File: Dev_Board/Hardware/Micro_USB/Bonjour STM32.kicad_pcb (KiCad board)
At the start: 2 copper layers, 50 x 70 mm, 68 parts, among them J11 IPS_SWITCH, Q1 S8050, Q2 S8050, Q3 S8050, SW1 SW_Push, SW2 SW_Push, SW3 SW_Push, U3 STM32F401RCTx

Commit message: Update PCB design
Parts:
- added G***: LOGO, Logo:emoe, B.Cu at (185.2, 104.5)
- added G***: LOGO, Logo:单片姬, F.Cu at (185.3, 83.0)
- added REF**: OSHW-Logo2_9.8x8mm_SilkScreen, Symbol:OSHW-Logo2_9.8x8mm_SilkScreen, B.Cu at (172.8, 63.5)
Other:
- board text added: "EEPROM"
- board text added: "Encoder"
- board text added: "FLASH"
- board text added: "I2C1"
- board text added: "I2C_2"
- board text added: "RX"
- board text added: "SPI1"
- board text added: "SPI_2"
- board text added: "TIM1_CH1/2"
- board text added: "TX"

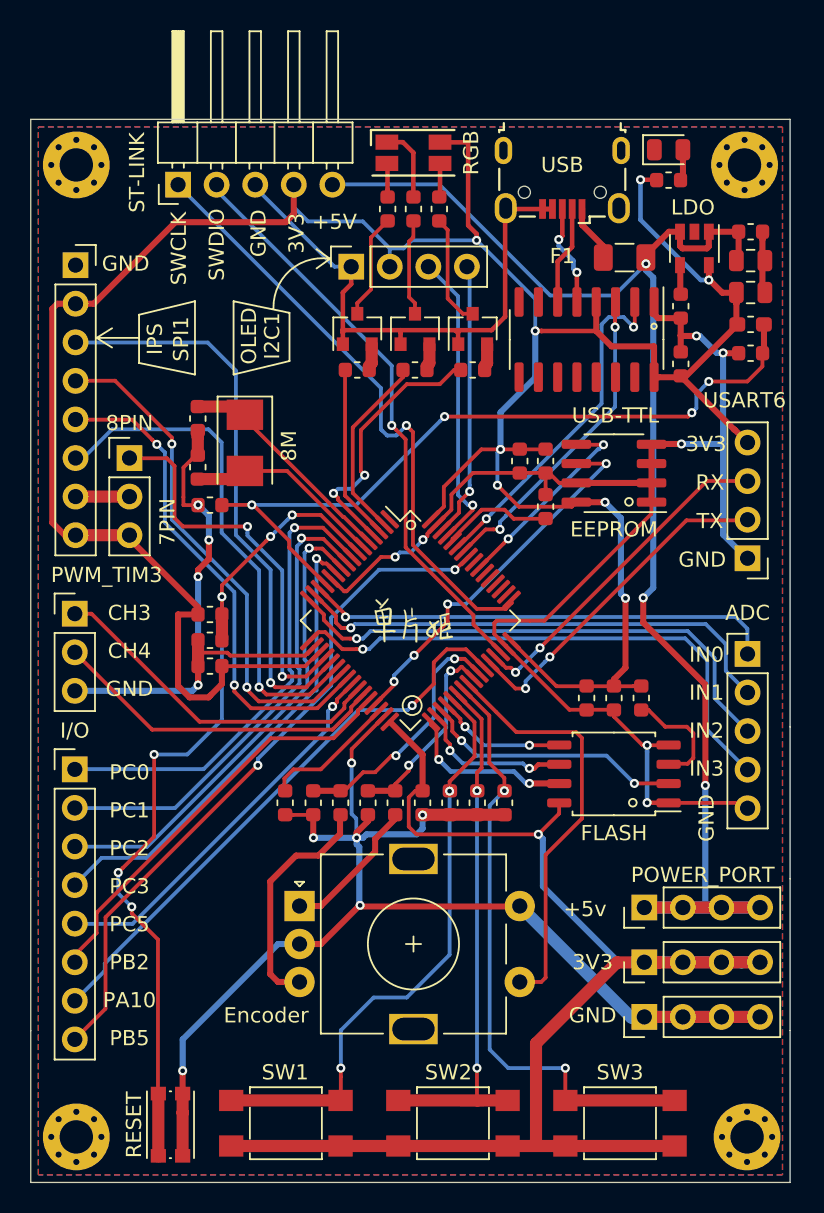
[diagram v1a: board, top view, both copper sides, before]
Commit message: fix footprint bug & add QR Code
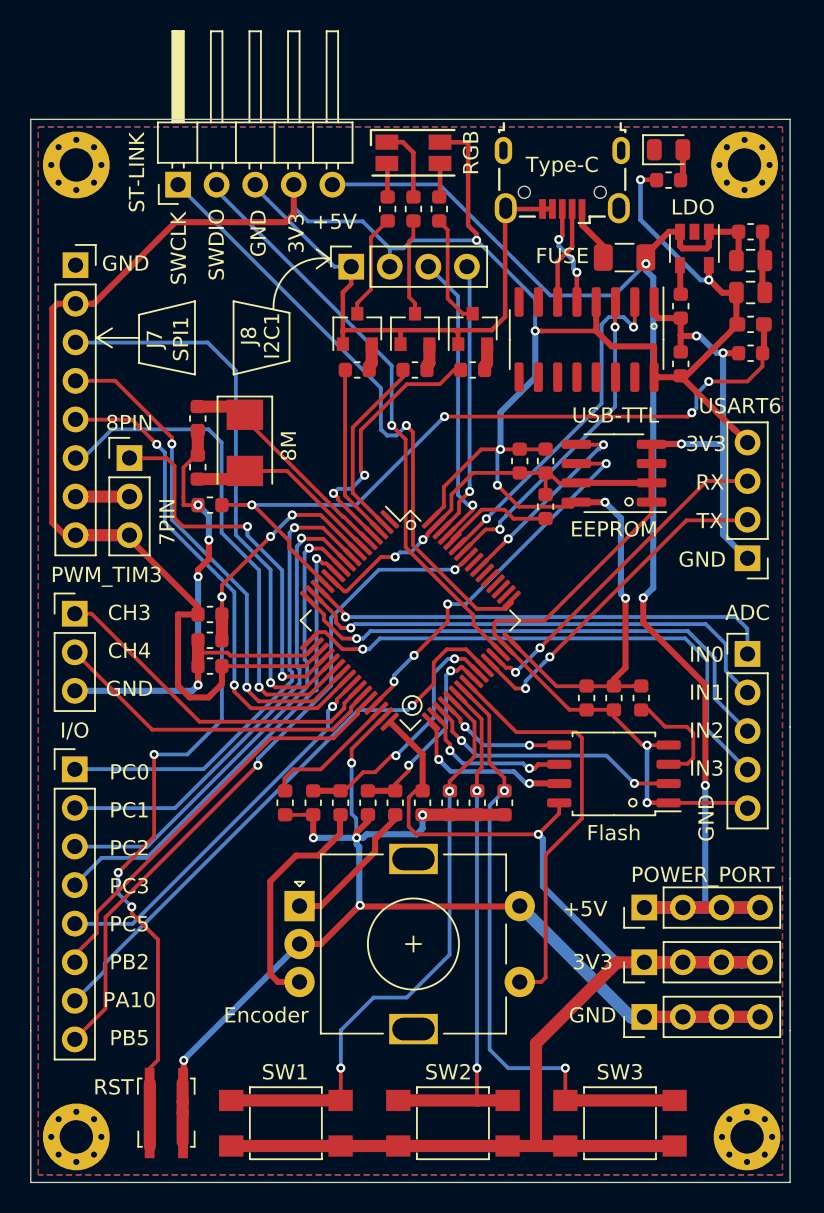
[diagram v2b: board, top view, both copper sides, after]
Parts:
- removed G***: LOGO, Logo:emoe
- removed G***: LOGO, Logo:单片姬
- removed REF**: OSHW-Logo2_9.8x8mm_SilkScreen, Symbol:OSHW-Logo2_9.8x8mm_SilkScreen
- RST: renamed from RESET; footprint Button_Switch_SMD:SW_Push_1P1T_NO_CK_KMR2 -> Button_Switch_SMD:Button_SMD_3mmx4mmx2.5mm
- moved RST 0.80 mm to (169.0, 115.4)
- renumbered +5v to +5V, F1 to FUSE, FLASH to Flash, IPS to J7, OLED to J8, USB to Type-C
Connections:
- Encoder pad MP: GND -> (no net)
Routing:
- net GND: track 270.7 -> 269.9 mm
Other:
- board text added: "TIM1_CH1&2"
- board text removed: "TIM1_CH1/2"

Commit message: Fix Fatal Error on PCB Design
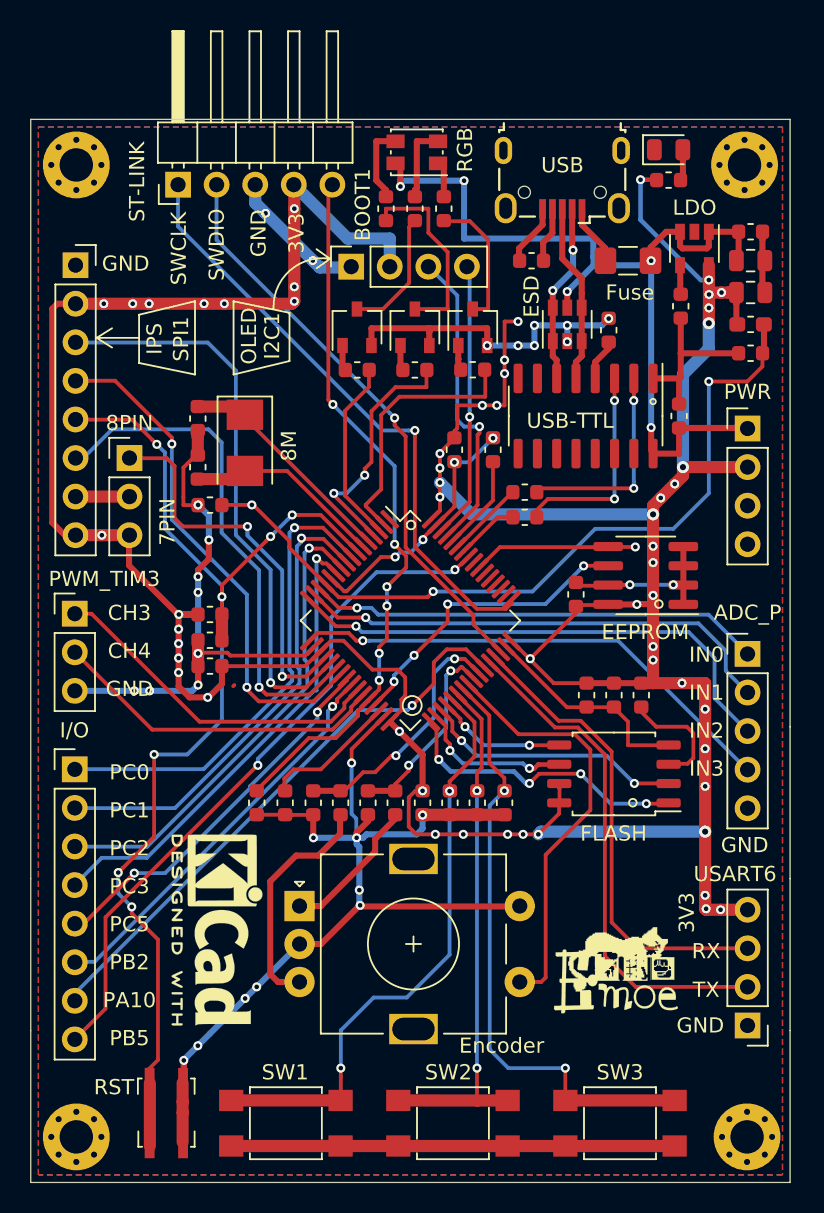
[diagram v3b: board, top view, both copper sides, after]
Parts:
- removed 3V3: 3V3, Connector_PinHeader_2.54mm:PinHeader_1x04_P2.54mm_Vertical
- removed GND: GND, Connector_PinHeader_2.54mm:PinHeader_1x04_P2.54mm_Vertical
- removed RGB: LED_RGBA, LED_SMD:LED_RGB_1210
- added C22: 104, Capacitor_SMD:C_0603_1608Metric, F.Cu at (202.7, 69.5)
- added D2: LED_RABG, LED_SMD:LED_Kingbright_AAA3528ESGCT, F.Cu at (185.4, 52.2)
- added G***: LOGO, Logo:emoe, F.Cu at (198.6, 106.3)
- added R12: 4.7k, Resistor_SMD:R_0603_1608Metric, F.Cu at (192.5, 76.2)
- added R13: 4.7k, Resistor_SMD:R_0603_1608Metric, F.Cu at (192.5, 74.5)
- added R14: 10k, Resistor_SMD:R_0603_1608Metric, F.Cu at (193.0, 59.3)
- added R15: 10k, Resistor_SMD:R_0603_1608Metric, F.Cu at (174.9, 95.0)
- added REF**: Symbol_GNU-Logo_SilkscreenTop, Symbol:Symbol_GNU-Logo_SilkscreenTop, B.Cu at (198.7, 103.8)
- added REF**: OSHW-Logo2_9.8x8mm_SilkScreen, Symbol:OSHW-Logo2_9.8x8mm_SilkScreen, B.Cu at (172.0, 106.6)
- added REF**: KiCad-Logo2_5mm_SilkScreen, Symbol:KiCad-Logo2_5mm_SilkScreen, F.Cu at (172.3, 103.4)
- added U6: USBLC6-2SC6, Package_TO_SOT_SMD:SOT-23-6, F.Cu at (195.3, 63.5)
- F1: renamed from FUSE; footprint Fuse:Fuse_1206_3216Metric -> Fuse:Fuse_1206_3216Metric_Pad1.42x1.75mm_HandSolder
- Q1, Q2, Q3: value S8050 -> S8050-SOT23; footprint Package_TO_SOT_SMD:SOT-23 -> Package_TO_SOT_SMD:SOT-23W
- moved J12 32.3 mm to (207.2, 70.4), turned to 0 degrees
- moved J6 30.8 mm to (207.2, 109.7)
- moved C20 9.00 mm to (195.9, 81.3), turned to 90 degrees
- moved U5 7.05 mm to (200.5, 80.0)
- moved C1 5.24 mm to (198.1, 63.9)
- moved R0 5.10 mm to (190.4, 71.8)
- moved U1 5.03 mm to (196.5, 69.5)
- moved C15 4.37 mm to (187.9, 71.8)
- moved Q3 3.81 mm to (185.3, 63.7)
- moved R10 3.81 mm to (185.3, 66.5), turned to 0 degrees
- moved Q1 3.80 mm to (189.1, 63.7)
- moved R5 3.80 mm to (189.1, 66.5), turned to 0 degrees
- moved R9 3.51 mm to (183.4, 55.9)
- moved R7 2.00 mm to (187.2, 55.9)
- moved R8 1.79 mm to (185.3, 55.9)
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- renumbered Type-C to J1, +5V to J12, ST-LINK to J13, ADC to J2, PWM_TIM3 to J3, I/O to J5, USART6 to J6, RST to SW4, Encoder to SW5, USB-TTL to U1, LDO to U2, Flash to U4, EEPROM to U5
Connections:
- C1 pad 1: +3V3 -> Net-(C1-Pad1)
- J1 pad 4: GND -> Net-(J1-Pad4)
- J12 pad 2: +5V -> +3V3
- J12 pad 3: +5V -> GND
- J12 pad 4: +5V -> GND
- J13 pad 5: +5V -> /BOOT1
- J5 pad 5: /PC5 -> /PC4
- J5 pad 6: /PB2 -> /PC5
- J7 pad 5: /SPI1_RST -> /NRST
- Q1 pad 1: GND -> Net-(Q1-Pad1)
- Q1 pad 2: Net-(Q1-Pad2) -> GND
- Q2 pad 1: GND -> Net-(Q2-Pad1)
- Q2 pad 2: Net-(Q2-Pad2) -> GND
- Q3 pad 1: GND -> Net-(Q3-Pad1)
- Q3 pad 2: Net-(Q3-Pad2) -> GND
- R10 pad 1: Net-(Q3-Pad2) -> Net-(Q3-Pad1)
- R5 pad 1: Net-(Q1-Pad2) -> Net-(Q1-Pad1)
- R6 pad 1: Net-(Q2-Pad2) -> Net-(Q2-Pad1)
- SW1 pad 1: +3V3 -> GND
- SW2 pad 1: +3V3 -> GND
- SW3 pad 1: +3V3 -> GND
- U1 pad 10: Net-(U1-Pad10) -> (no net)
- U1 pad 11: Net-(U1-Pad11) -> (no net)
- U1 pad 12: Net-(U1-Pad12) -> (no net)
- U1 pad 13: Net-(U1-Pad13) -> (no net)
- U1 pad 14: Net-(U1-Pad14) -> (no net)
- U1 pad 15: Net-(U1-Pad15) -> (no net)
- U1 pad 16: +3V3 -> +5V
- U1 pad 2: /USART1_RX -> Net-(R13-Pad1)
- U1 pad 3: /USART1_TX -> Net-(R12-Pad1)
- U1 pad 4: +3V3 -> Net-(C1-Pad1)
- U1 pad 7: Net-(U1-Pad7) -> (no net)
- U1 pad 8: Net-(U1-Pad8) -> (no net)
- U1 pad 9: Net-(U1-Pad9) -> (no net)
- U3 pad 1: /VBAT -> (no net)
- U3 pad 24: /SPI1_RST -> /PC4
- U3 pad 28: /PB2 -> /BOOT1
- U3 pad 33: /SPI2_HOLD -> /SPI2_CS
- U3 pad 50: /SPI3_DC -> (no net)
- U3 pad 51: /SPI3_SCK -> (no net)
- U3 pad 52: /SPI3_MISO -> (no net)
- U3 pad 53: /SPI3_MOSI -> (no net)
- U3 pad 54: /SPI3_CS -> (no net)
- U3 pad 56: /SPI3_RST -> (no net)
- U4 pad 1: GND -> /SPI2_CS
- U4 pad 7: /SPI2_HOLD -> +3V3
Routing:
- net /BOOT1: track 0.00 -> 47.2 mm, vias 0 -> 6
- net GND: track 269.9 -> 226.7 mm, vias 17 -> 33
- net +3V3: track 284.1 -> 242.2 mm, vias 9 -> 56
- net +5V: track 94.8 -> 58.8 mm, vias 3 -> 5
- net /SPI1_RST: track 33.2 -> 0.00 mm, vias 2 -> 0
- net /PB2: track 27.7 -> 0.00 mm
- net /PC4: track 0.00 -> 25.1 mm, vias 0 -> 2
- net /SPI2_CS: track 0.00 -> 19.8 mm, vias 0 -> 4
- net /NRST: track 57.3 -> 75.1 mm, vias 6 -> 7
- net /USART1_RX: track 22.9 -> 5.17 mm, vias 2 -> 0
- net /USART1_TX: track 21.2 -> 4.22 mm, vias 2 -> 0
- net Net-(R13-Pad1): track 0.00 -> 13.9 mm, vias 0 -> 2
- net Net-(R12-Pad1): track 0.00 -> 13.9 mm, vias 0 -> 2
- net /SPI2_HOLD: track 11.2 -> 0.00 mm, vias 2 -> 0
- net /USART6_TX: track 22.5 -> 33.6 mm, vias 2 -> 0
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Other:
- board text added: "ADC_P"
- board text added: "BOOT1"
- board text added: "ESD"
- board text added: "Fuse"
- board text added: "I/O"
- board text added: "IPS"
- board text added: "LDO"
- board text added: "OLED"
- board text added: "PWM_TIM3"
- board text added: "PWR"
- board text added: "RGB"
- board text added: "RST"
- board text added: "ST-LINK"
- board text added: "USB"
- board text added: "USB-TTL"
- board text removed: "+5V"
- board text removed: "POWER_PORT"
